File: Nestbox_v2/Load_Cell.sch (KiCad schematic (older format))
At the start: 33 parts, among them J601 LOAD_CELL_CONN_01X04, Q601 DMG2301L-7 -- Replace by 0R, Q602 DMG3402L DNP, Q603 DMG2301L-7 DNP, Q604 DMG3402L DNP, U601 ADS1220

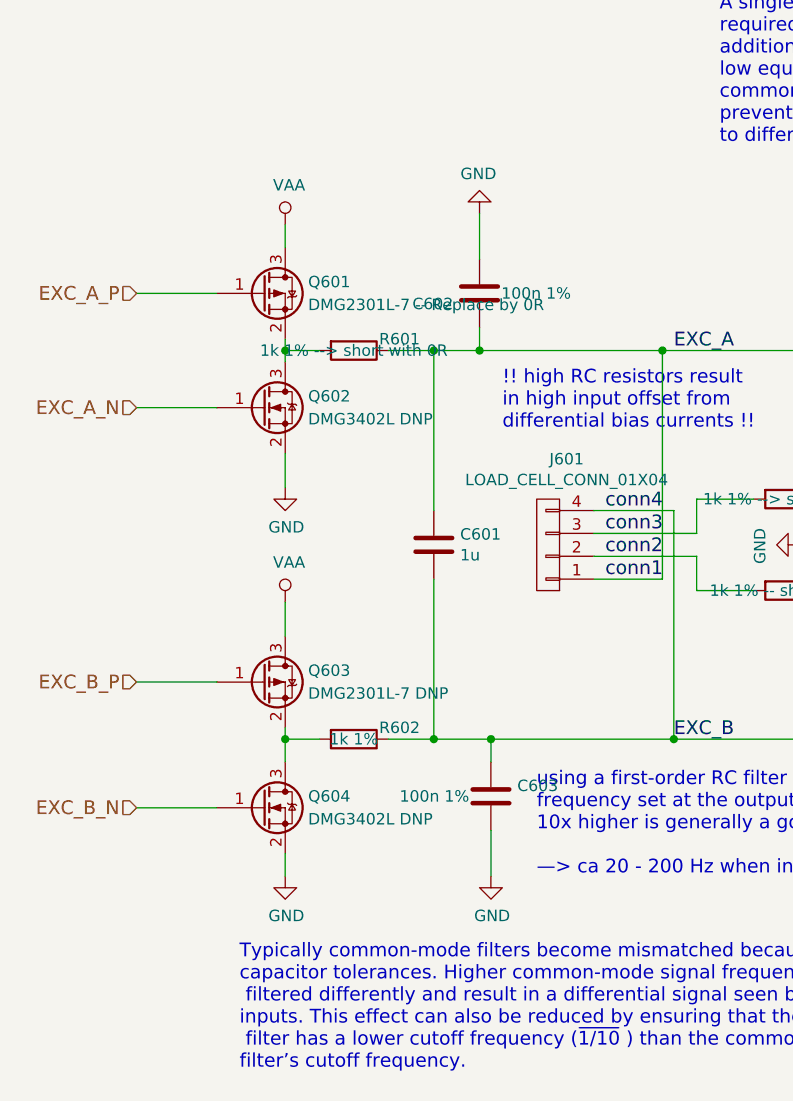
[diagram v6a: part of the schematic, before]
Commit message: TAPEOUT second batch nestbox main + EM pcb. added pull-ups, corrected pmos of load cell, WIFI AND SDCARD ENABLE PMOS ARE STILL WRONGLY ORIENTED
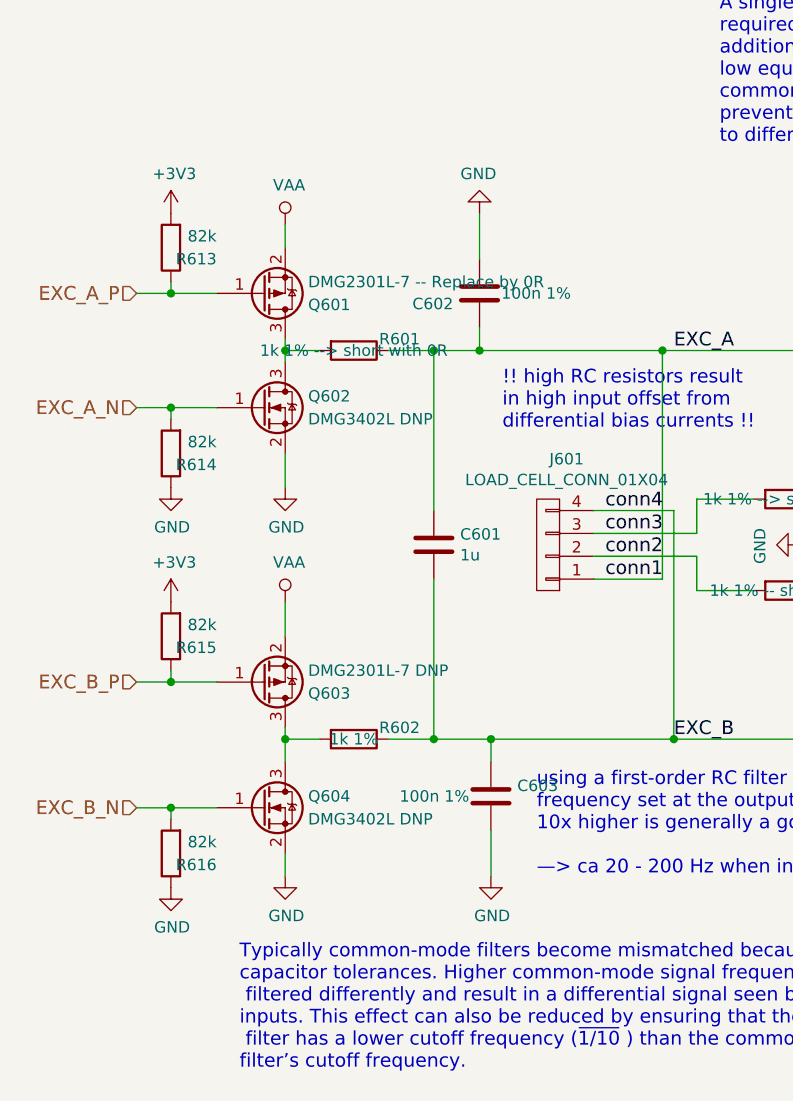
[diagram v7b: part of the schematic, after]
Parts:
- added R613, R614, R615, R616: 82k, Resistors_SMD:R_0603, symbol R
- C610: footprint Capacitors_SMD:C_0603 -> Capacitors_SMD:C_0805
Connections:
- wire segments 86 -> 90
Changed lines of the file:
@@
 $EndDescr
 $Comp
-L +3V3 #PWR615
+L +3V3 #PWR619
 U 1 1 5AF731D8
 P 7950 2900
-F 0 "#PWR615" H 7950 2750 50  0001 C CNN
+F 0 "#PWR619" H 7950 2750 50  0001 C CNN
 F 1 "+3V3" H 7965 3073 50  0000 C CNN
 F 2 "" H 7950 2900 50  0001 C CNN
@@
 F 0 "C610" V 8198 3100 50  0000 C CNN
 F 1 "10u" V 8289 3100 50  0000 C CNN
-F 2 "Capacitors_SMD:C_0603" H 8488 2950 50  0001 C CNN
+F 2 "Capacitors_SMD:C_0805" H 8488 2950 50  0001 C CNN
 F 3 "" H 8450 3100 50  0001 C CNN
 	1    8450 3100
@@
 $EndComp
 $Comp
-L GND #PWR616
+L GND #PWR620
 U 1 1 5AF734D9
 P 7950 4600
-F 0 "#PWR616" H 7950 4350 50  0001 C CNN
+F 0 "#PWR620" H 7950 4350 50  0001 C CNN
 F 1 "GND" H 7955 4427 50  0000 C CNN
 F 2 "" H 7950 4600 50  0001 C CNN
@@
 $EndComp
 $Comp
-L GND #PWR618
+L GND #PWR622
 U 1 1 5AF737C3
 P 8050 4600
-F 0 "#PWR618" H 8050 4350 50  0001 C CNN
+F 0 "#PWR622" H 8050 4350 50  0001 C CNN
 F 1 "GND" H 8055 4427 50  0000 C CNN
 F 2 "" H 8050 4600 50  0001 C CNN
@@
 $EndComp
 $Comp
-L GND #PWR619
+L GND #PWR623
 U 1 1 5AF737DA
 P 8650 3100
-F 0 "#PWR619" H 8650 2850 50  0001 C CNN
+F 0 "#PWR623" H 8650 2850 50  0001 C CNN
 F 1 "GND" V 8655 2972 50  0000 R CNN
 F 2 "" H 8650 3100 50  0001 C CNN
@@
 $EndComp
 $Comp
-L GND #PWR620
+L GND #PWR624
 U 1 1 5AF73803
 P 8650 3350
-F 0 "#PWR620" H 8650 3100 50  0001 C CNN
+F 0 "#PWR624" H 8650 3100 50  0001 C CNN
 F 1 "GND" V 8655 3222 50  0000 R CNN
 F 2 "" H 8650 3350 50  0001 C CNN
@@
 $EndComp
 $Comp
-L GND #PWR614
+L GND #PWR618
 U 1 1 5AF73B67
 P 7450 3400
-F 0 "#PWR614" H 7450 3150 50  0001 C CNN
+F 0 "#PWR618" H 7450 3150 50  0001 C CNN
 F 1 "GND" V 7455 3272 50  0000 R CNN
 F 2 "" H 7450 3400 50  0001 C CNN
@@
 $EndComp
 $Comp
-L GND #PWR613
+L GND #PWR617
 U 1 1 5AF73BBF
 P 7450 3100
-F 0 "#PWR613" H 7450 2850 50  0001 C CNN
+F 0 "#PWR617" H 7450 2850 50  0001 C CNN
 F 1 "GND" V 7455 2972 50  0000 R CNN
 F 2 "" H 7450 3100 50  0001 C CNN
@@
 $EndComp
 $Comp
-L GND #PWR610
+L GND #PWR614
 U 1 1 5AF756EC
 P 4400 4000
-F 0 "#PWR610" H 4400 3750 50  0001 C CNN
+F 0 "#PWR614" H 4400 3750 50  0001 C CNN
 F 1 "GND" H 4405 3827 50  0000 C CNN
 F 2 "" H 4400 4000 50  0001 C CNN
@@
 $EndComp
 $Comp
-L GND #PWR607
+L GND #PWR611
 U 1 1 5AF75761
 P 3900 4000
-F 0 "#PWR607" H 3900 3750 50  0001 C CNN
+F 0 "#PWR611" H 3900 3750 50  0001 C CNN
 F 1 "GND" H 3905 3827 50  0000 C CNN
 F 2 "" H 3900 4000 50  0001 C CNN
@@
 $EndComp
 $Comp
-L GND #PWR621
+L GND #PWR625
 U 1 1 5AF76892
 P 8800 4350
-F 0 "#PWR621" H 8800 4100 50  0001 C CNN
+F 0 "#PWR625" H 8800 4100 50  0001 C CNN
 F 1 "GND" H 8805 4177 50  0000 C CNN
 F 2 "" H 8800 4350 50  0001 C CNN
@@
 EXC_B
 $Comp
-L GND #PWR602
+L GND #PWR606
 U 1 1 5AF8B9E6
 P 1650 3750
-F 0 "#PWR602" H 1650 3500 50  0001 C CNN
+F 0 "#PWR606" H 1650 3500 50  0001 C CNN
 F 1 "GND" H 1655 3577 50  0000 C CNN
 F 2 "" H 1650 3750 50  0001 C CNN
@@
 $EndComp
 $Comp
-L GND #PWR604
+L GND #PWR608
 U 1 1 5AF8BA1F
 P 1650 5450
-F 0 "#PWR604" H 1650 5200 50  0001 C CNN
+F 0 "#PWR608" H 1650 5200 50  0001 C CNN
 F 1 "GND" H 1655 5277 50  0000 C CNN
 F 2 "" H 1650 5450 50  0001 C CNN
@@
 $EndComp
 $Comp
-L VAA #PWR601
+L VAA #PWR605
 U 1 1 5AF8BE8C
 P 1650 2600
-F 0 "#PWR601" H 1650 2450 50  0001 C CNN
+F 0 "#PWR605" H 1650 2450 50  0001 C CNN
 F 1 "VAA" H 1667 2773 50  0000 C CNN
 F 2 "" H 1650 2600 50  0001 C CNN
@@
 $EndComp
 $Comp
-L VAA #PWR603
+L VAA #PWR607
 U 1 1 5AF8C0F0
 P 1650 4250
-F 0 "#PWR603" H 1650 4100 50  0001 C CNN
+F 0 "#PWR607" H 1650 4100 50  0001 C CNN
 F 1 "VAA" H 1667 4423 50  0000 C CNN
 F 2 "" H 1650 4250 50  0001 C CNN
@@
 $EndComp
 $Comp
-L VAA #PWR617
+L VAA #PWR621
 U 1 1 5AF8C129
 P 8050 2550
-F 0 "#PWR617" H 8050 2400 50  0001 C CNN
+F 0 "#PWR621" H 8050 2400 50  0001 C CNN
 F 1 "VAA" H 8067 2723 50  0000 C CNN
 F 2 "" H 8050 2550 50  0001 C CNN
@@
 $EndComp
 $Comp
-L GND #PWR606
+L GND #PWR610
 U 1 1 5AF8D573
 P 2550 5450
-F 0 "#PWR606" H 2550 5200 50  0001 C CNN
+F 0 "#PWR610" H 2550 5200 50  0001 C CNN
 F 1 "GND" H 2555 5277 50  0000 C CNN
 F 2 "" H 2550 5450 50  0001 C CNN
@@
 $EndComp
 $Comp
-L GND #PWR605
+L GND #PWR609
 U 1 1 5AF8D7AF
 P 2500 2550
-F 0 "#PWR605" H 2500 2300 50  0001 C CNN
+F 0 "#PWR609" H 2500 2300 50  0001 C CNN
 F 1 "GND" H 2505 2377 50  0000 C CNN
 F 2 "" H 2500 2550 50  0001 C CNN
@@
 $EndComp
 $Comp
-L GND #PWR612
+L GND #PWR616
 U 1 1 5AF97D06
 P 6100 4000
-F 0 "#PWR612" H 6100 3750 50  0001 C CNN
+F 0 "#PWR616" H 6100 3750 50  0001 C CNN
 F 1 "GND" H 6105 3827 50  0000 C CNN
 F 2 "" H 6100 4000 50  0001 C CNN
@@
 $EndComp
 $Comp
-L GND #PWR611
+L GND #PWR615
 U 1 1 5AF97F53
 P 5600 4000
-F 0 "#PWR611" H 5600 3750 50  0001 C CNN
+F 0 "#PWR615" H 5600 3750 50  0001 C CNN
 F 1 "GND" H 5605 3827 50  0000 C CNN
 F 2 "" H 5600 4000 50  0001 C CNN
@@
 LIGHTBARRIER_LED_OUTPUT
 $Comp
-L +3.3V #PWR608
+L +3.3V #PWR612
 U 1 1 5B145174
 P 3950 6750
-F 0 "#PWR608" H 3950 6600 50  0001 C CNN
+F 0 "#PWR612" H 3950 6600 50  0001 C CNN
 F 1 "+3.3V" H 3950 6890 50  0000 C CNN
 F 2 "" H 3950 6750 50  0001 C CNN
@@
 $EndComp
 $Comp
-L GND #PWR609
+L GND #PWR613
 U 1 1 5B14520C
 P 3950 7050
-F 0 "#PWR609" H 3950 6800 50  0001 C CNN
+F 0 "#PWR613" H 3950 6800 50  0001 C CNN
 F 1 "GND" H 3950 6900 50  0000 C CNN
 F 2 "" H 3950 7050 50  0001 C CNN
@@
 F 3 "" H 1550 4600 50  0001 C CNN
 	1    1550 4600
-	1    0    0    -1
+	1    0    0    1
 $EndComp
 $Comp
@@
 F 3 "" H 1550 2900 50  0001 C CNN
 	1    1550 2900
-	1    0    0    -1
+	1    0    0    1
 $EndComp
 $Comp
@@
 	1    0    0    -1
 $EndComp
+$Comp
+L R R616
+U 1 1 5B298376
+P 1150 5350
+F 0 "R616" H 950 5400 50  0000 L CNN
+F 1 "82k" H 950 5300 50  0000 L CNN
+F 2 "Resistors_SMD:R_0603" V 1080 5350 50  0001 C CNN
+F 3 "" H 1150 5350 50  0001 C CNN
+	1    1150 5350
+	-1   0    0    1
+$EndComp
+$Comp
+L R R615
+U 1 1 5B298604
+P 1150 4400
+F 0 "R615" H 950 4450 50  0000 L CNN
+F 1 "82k" H 950 4350 50  0000 L CNN
+F 2 "Resistors_SMD:R_0603" V 1080 4400 50  0001 C CNN
+F 3 "" H 1150 4400 50  0001 C CNN
+	1    1150 4400
+	-1   0    0    1
+$EndComp
+$Comp
+L R R614
+U 1 1 5B298689
+P 1150 3600
+F 0 "R614" H 950 3650 50  0000 L CNN
+F 1 "82k" H 950 3550 50  0000 L CNN
+F 2 "Resistors_SMD:R_0603" V 1080 3600 50  0001 C CNN
+F 3 "" H 1150 3600 50  0001 C CNN
+	1    1150 3600
+	-1   0    0    1
+$EndComp
+$Comp
+L R R613
+U 1 1 5B298714
+P 1150 2700
+F 0 "R613" H 950 2750 50  0000 L CNN
+F 1 "82k" H 950 2650 50  0000 L CNN
+F 2 "Resistors_SMD:R_0603" V 1080 2700 50  0001 C CNN
+F 3 "" H 1150 2700 50  0001 C CNN
+	1    1150 2700
+	-1   0    0    1
+$EndComp
+$Comp
+L GND #PWR604
+U 1 1 5B29879E
+P 1150 5500
+F 0 "#PWR604" H 1150 5250 50  0001 C CNN
+F 1 "GND" H 1155 5327 50  0000 C CNN
+F 2 "" H 1150 5500 50  0001 C CNN
+F 3 "" H 1150 5500 50  0001 C CNN
+	1    1150 5500
+	1    0    0    -1
+$EndComp
+Wire Wire Line
+	1150 5200 1150 5150
+Connection ~ 1150 5150
+Wire Wire Line
+	1150 4600 1150 4550
+Connection ~ 1150 4600
+Wire Wire Line
+	1150 3450 1150 3400
+Connection ~ 1150 3400
+$Comp
+L GND #PWR602
+U 1 1 5B298A71
+P 1150 3750
+F 0 "#PWR602" H 1150 3500 50  0001 C CNN
+F 1 "GND" H 1155 3577 50  0000 C CNN
+F 2 "" H 1150 3750 50  0001 C CNN
+F 3 "" H 1150 3750 50  0001 C CNN
+	1    1150 3750
+	1    0    0    -1
+$EndComp
+Wire Wire Line
+	1150 2850 1150 2900
+Connection ~ 1150 2900
+$Comp
+L +3V3 #PWR601
+U 1 1 5B298E8F
+P 1150 2550
+F 0 "#PWR601" H 1150 2400 50  0001 C CNN
+F 1 "+3V3" H 1165 2723 50  0000 C CNN
+F 2 "" H 1150 2550 50  0001 C CNN
+F 3 "" H 1150 2550 50  0001 C CNN
+	1    1150 2550
+	1    0    0    -1
+$EndComp
+$Comp
+L +3V3 #PWR603
+U 1 1 5B298FE7
+P 1150 4250
+F 0 "#PWR603" H 1150 4100 50  0001 C CNN
+F 1 "+3V3" H 1165 4423 50  0000 C CNN
+F 2 "" H 1150 4250 50  0001 C CNN
+F 3 "" H 1150 4250 50  0001 C CNN
+	1    1150 4250
+	1    0    0    -1
+$EndComp
